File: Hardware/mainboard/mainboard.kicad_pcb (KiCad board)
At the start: 2 copper layers, 45 parts, among them J1 559592430, J2 B4B-EH-A, J3 B4B-EH-A, J4 B05B-XASK-1LFSN, J5 RST, J6 Conn_01x06_Socket, J7 SBH11-PBPC-D05-ST-BK, J9 USB_C_Receptacle_PowerOnly_24P, SW2 BOT, SW3 BOOT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

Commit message: pushing for the evening
didnt add much, just moved things around and fixed footprints
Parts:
- removed J5: RST, 1x02_jst_conn:CONN_B02B-XASK-1LFSN_JST
- added SW1: ON-BOARD, Button_Switch_SMD:SW_Tactile_SPST_NO_Straight_CK_PTS636Sx25SMTRLFS, F.Cu at (172.7, 86.4)
- SW3: footprint Connector_PinHeader_1.00mm:PinHeader_1x03_P1.00mm_Vertical -> Connector_PinHeader_2.54mm:PinHeader_1x03_P2.54mm_Vertical
- moved J2 148.0 mm to (229.9, 53.3), turned to 0 degrees
- moved J6 146.6 mm to (265.4, 87.2)
- moved R12 113.6 mm to (102.9, 60.0), turned to 90 degrees
- moved R1 110.3 mm to (232.4, 121.9), turned to 180 degrees
- moved U1 108.2 mm to (73.4, 138.9), turned to -90 degrees
- moved R11 107.5 mm to (102.9, 65.0), turned to 90 degrees
- moved R10 101.6 mm to (102.9, 70.1), turned to 90 degrees
- moved C8 98.6 mm to (152.7, 30.5), turned to 0 degrees
- moved R9 95.9 mm to (102.8, 75.2), turned to 90 degrees
- moved C7 95.0 mm to (147.6, 30.5), turned to 0 degrees
- moved C6 91.5 mm to (142.6, 30.5), turned to 0 degrees
- moved C5 87.9 mm to (137.5, 30.5), turned to 0 degrees
- moved C14 71.6 mm to (118.4, 150.6)
- moved J9 63.3 mm to (221.7, 149.9)
- moved D3 59.0 mm to (223.5, 139.7)
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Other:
- board text added: "3v3"
- board text added: "5v"
- board text added: "IR LEDs"
- board text added: "debouncing"
- board text added: "osc"
- board text added: "power in"
- board text added: "programming"
- board text added: "reset"
- board text added: "status led smd"

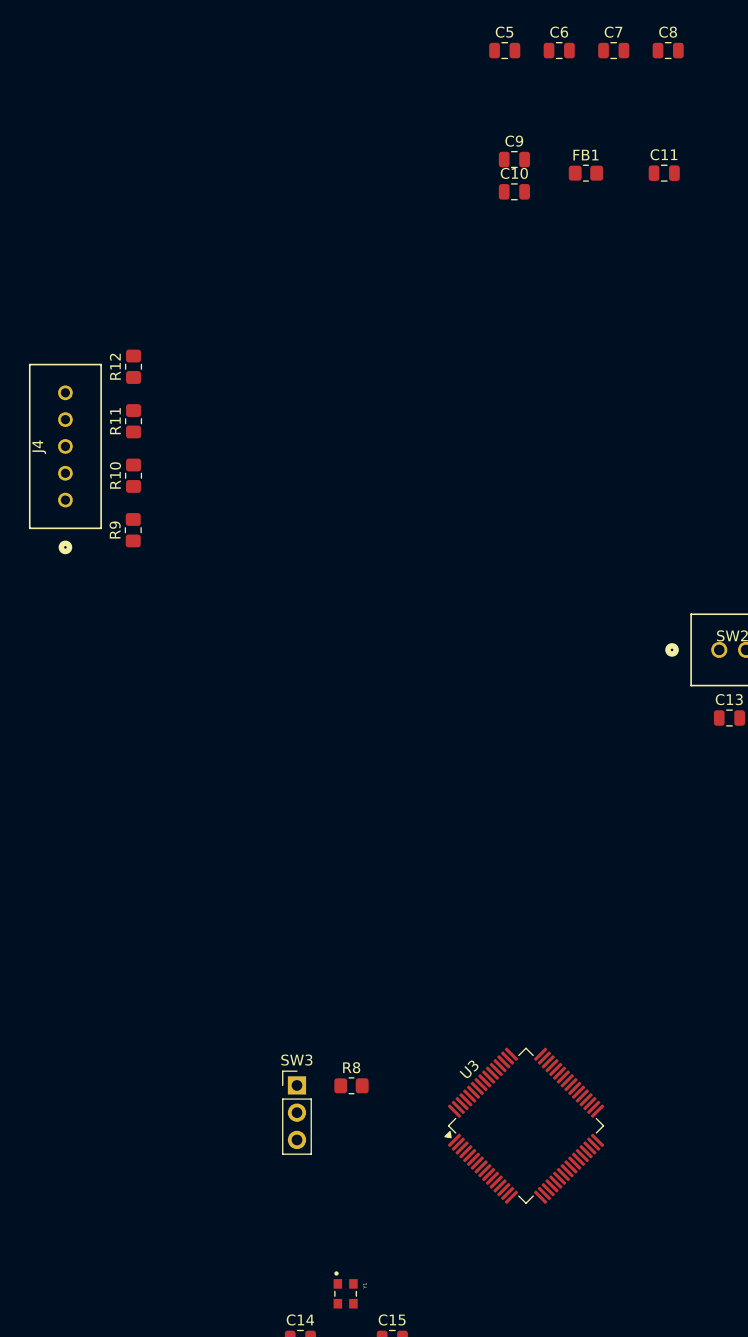
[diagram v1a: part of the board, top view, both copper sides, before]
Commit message: Lowkey forgot the start switch so i added that
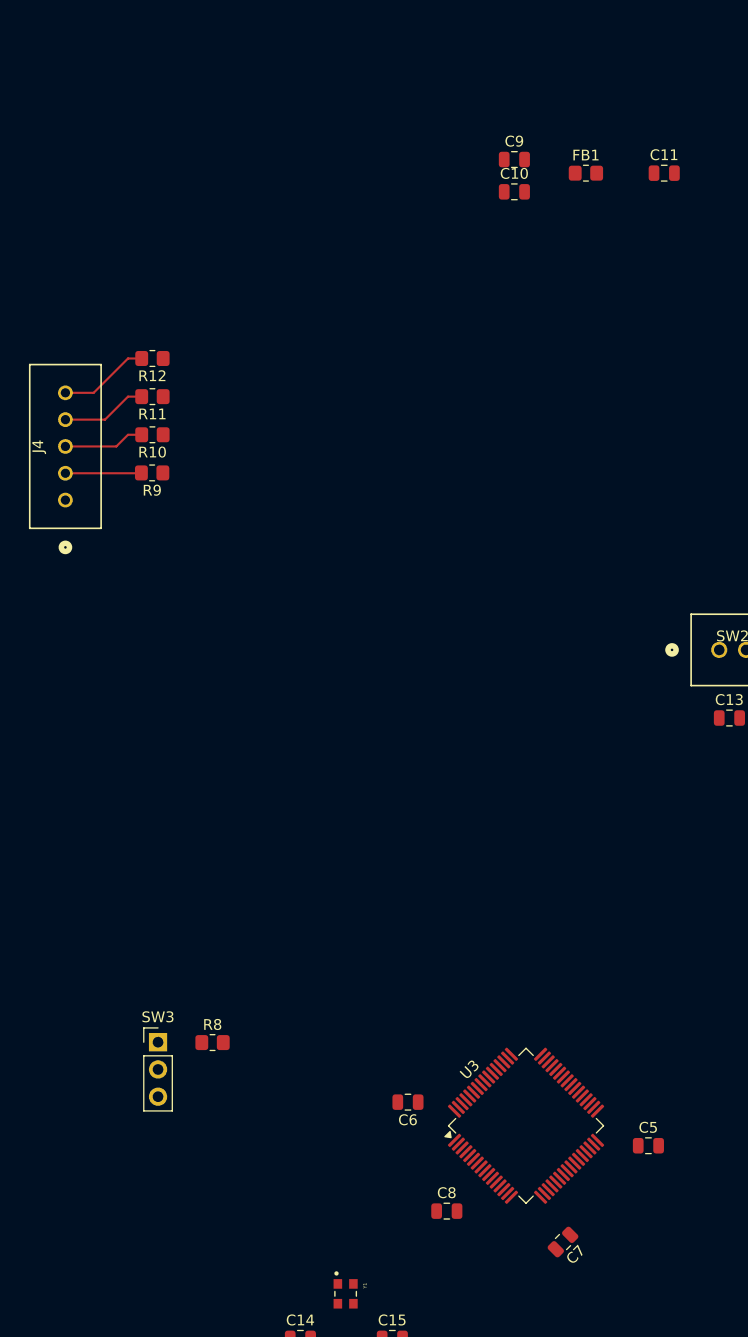
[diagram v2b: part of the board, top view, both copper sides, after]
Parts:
- moved C7 111.2 mm to (142.9, 141.6), turned to -135 degrees
- moved C8 110.2 mm to (132.1, 138.7)
- moved C5 103.0 mm to (150.9, 132.6)
- moved C6 99.1 mm to (128.5, 128.5), turned to 180 degrees
- moved R8 13.6 mm to (110.2, 123.0)
- moved SW3 13.6 mm to (105.2, 122.9)
- moved R9 5.63 mm to (104.6, 69.9), turned to 180 degrees
- moved R10 4.21 mm to (104.6, 66.3), turned to 180 degrees
- moved R11 2.89 mm to (104.6, 62.7), turned to 180 degrees
- moved R12 1.92 mm to (104.6, 59.2), turned to 180 degrees
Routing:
- net IR_4: track 0.00 -> 8.59 mm
- net IR_3: track 0.00 -> 8.15 mm
- net IR_2: track 0.00 -> 7.71 mm
- net IR_1: track 0.00 -> 7.25 mm

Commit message: layout
worked on the layput but im actively falling asleep while working on it so im going to call it a day
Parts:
- C1, C12, C13, C6, C7, C8: value C -> 100nF
- C10, C11: value C -> 1uF
- C14, C15: value C -> 10pF
- C2, C5: value C -> 10uF
- C3, C4: value C -> 22uF
- C9: value C -> 10nF
- D1, D3: value SMAZ5V1-13-F -> zener
- J6: footprint Connector_PinHeader_1.00mm:PinHeader_1x06_P1.00mm_Vertical -> Connector_PinHeader_2.54mm:PinHeader_1x06_P2.54mm_Vertical
- R1: value R_US -> 1k5
- R10, R11, R12, R9: value R_US -> 220
- R2, R3, R4, R5, R6, R7: value R_US -> 50
- R8: value R_US -> 10k
- moved J7 141.7 mm to (134.6, 174.0)
- moved D2 129.7 mm to (110.5, 160.1), turned to -90 degrees
- moved R1 126.3 mm to (110.5, 154.7), turned to -90 degrees
- moved J1 110.6 mm to (170.2, 138.3), turned to -90 degrees
- moved J6 110.1 mm to (156.0, 98.6)
- moved U2 99.1 mm to (119.4, 157.5), turned to 180 degrees
- moved U1 94.7 mm to (167.6, 129.9), turned to 90 degrees
- moved D1 94.4 mm to (143.5, 162.6), turned to -90 degrees
- moved C3 88.1 mm to (128.3, 153.7), turned to 90 degrees
- moved C4 85.4 mm to (128.3, 159.1), turned to -90 degrees
- moved C2 83.8 mm to (142.2, 154.9)
- moved C1 82.6 mm to (148.6, 154.9)
- moved D3 74.7 mm to (152.4, 162.6), turned to -90 degrees
- moved J4 73.8 mm to (100.3, 146.1)
- moved R9 73.8 mm to (108.4, 143.6)
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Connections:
- U3 pad 52: unconnected-(U3-PC11-Pad52) -> PC11
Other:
- board text removed: "osc"

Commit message: add layer
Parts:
- removed J9: USB_C_Receptacle_PowerOnly_24P, usbc_power_only:KUSBX-SMT-CS-6-BTR_KYC
- removed R10, R11, R12, R9: 220, Resistor_SMD:R_0805_2012Metric_Pad1.20x1.40mm_HandSolder
- removed R2, R3, R4, R5, R6, R7: 50, Resistor_SMD:R_0805_2012Metric_Pad1.20x1.40mm_HandSolder
- added J5: race start, BIG LIBRARY:1X03_JST, F.Cu at (156.0, 108.0)
- added J8: KUSBX-SMT-CS-6-BTR, usbc_power_only:KUSBX-SMT-CS-6-BTR_KYC, F.Cu at (100.5, 169.0)
- added R13: R_US, Resistor_SMD:R_0805_2012Metric_Pad1.20x1.40mm_HandSolder, F.Cu at (153.2, 113.5)
- added TP1: TestPoint, TestPoint:TestPoint_Keystone_5019_Minature, F.Cu at (65.0, 58.1)
- added TP2: TestPoint, TestPoint:TestPoint_Keystone_5019_Minature, F.Cu at (65.0, 62.0)
- added TP3: TestPoint, TestPoint:TestPoint_Keystone_5019_Minature, F.Cu at (65.0, 66.0)
- C6, C7, C8: moved to B.Cu
- J2: value B4B-EH-A -> status bot
- J3: value B4B-EH-A -> status eot
- J6: value Conn_01x06_Socket -> usb-ttl
- J7: value SBH11-PBPC-D05-ST-BK -> jtag
- U3: footprint Package_QFP:LQFP-64_10x10mm_P0.5mm -> STM32F091RCT-6:STM32F091RCT6-M
- moved J3 137.6 mm to (99.0, 111.0), turned to 90 degrees
- moved J2 136.7 mm to (106.0, 111.0), turned to 90 degrees
- moved C11 107.9 mm to (128.0, 147.0), turned to 90 degrees
- moved FB1 107.0 mm to (132.8, 148.2), turned to 180 degrees
- moved C9 102.9 mm to (130.2, 143.2), turned to 90 degrees
- moved C10 99.7 mm to (134.8, 143.2), turned to 90 degrees
- moved J6 75.8 mm to (91.0, 137.5), turned to 180 degrees
- moved SW2 63.4 mm to (159.6, 149.3), turned to -90 degrees
- moved J1 60.0 mm to (119.5, 106.2), turned to 0 degrees
- moved J7 54.6 mm to (100.5, 131.3), turned to -90 degrees
- moved D3 52.7 mm to (99.9, 158.4), turned to 180 degrees
- moved C13 49.1 mm to (152.0, 150.1), turned to 90 degrees
- moved SW1 48.5 mm to (158.9, 160.0), turned to 0 degrees
- moved D1 45.1 mm to (99.9, 151.0), turned to 180 degrees
- moved C1 41.2 mm to (107.5, 153.0), turned to -90 degrees
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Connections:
- C10 pad 2: GND -> Net-(U3-VDDA)
- C9 pad 2: GND -> Net-(U3-VDDA)
- U3 pad 13: GND -> Net-(U3-VDDA)
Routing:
- net PB10: track 0.00 -> 52.4 mm, vias 0 -> 2
- net SWDIO: track 0.00 -> 48.0 mm
- net SWCLK: track 0.00 -> 47.9 mm
- net PC11: track 0.00 -> 31.1 mm, vias 0 -> 2
- net PA0: track 0.00 -> 27.2 mm
- net PA2: track 0.00 -> 26.0 mm
- net PA1: track 0.00 -> 26.0 mm
- net PA7: track 0.00 -> 22.9 mm
- net PA6: track 0.00 -> 22.5 mm
- net PA5: track 0.00 -> 22.1 mm
- net PA3: track 0.00 -> 21.8 mm
- net PA4: track 0.00 -> 21.6 mm
- net PC10: track 0.00 -> 17.8 mm, vias 0 -> 1
- net Net-(U3-VDDA): track 0.00 -> 11.4 mm
- net +3.3V: track 0.00 -> 10.3 mm, vias 0 -> 3
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- added copper zone on In2.Cu, net +3.3V
- added copper zone on B.Cu, net GND
- added copper zone on F.Cu, net GND
- added copper zone on In1.Cu, net GND
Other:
- copper layers 2 -> 4

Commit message: routed traces
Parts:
- added REF**: MountingHole_4.3mm_M4, MountingHole:MountingHole_4.3mm_M4, F.Cu at (135.6, 85.9)
- added REF**: MountingHole_4.3mm_M4, MountingHole:MountingHole_4.3mm_M4, F.Cu at (66.3, 25.4)
- added REF**: MountingHole_4.3mm_M4, MountingHole:MountingHole_4.3mm_M4, F.Cu at (66.4, 85.9)
- added REF**: MountingHole_4.3mm_M4, MountingHole:MountingHole_4.3mm_M4, F.Cu at (135.6, 25.5)
- moved J6 93.5 mm to (65.3, 47.6), turned to 0 degrees
- moved C12 89.1 mm to (119.4, 75.9), turned to 180 degrees
- moved D2 88.1 mm to (92.8, 86.0)
- moved R1 88.1 mm to (87.4, 86.0)
- moved U2 88.1 mm to (90.2, 77.1)
- moved J4 87.7 mm to (103.1, 85.7)
- moved C3 86.9 mm to (86.7, 69.3)
- moved C4 86.9 mm to (92.1, 69.3)
- moved C5 86.9 mm to (92.1, 64.2)
- moved SW1 85.7 mm to (125.0, 81.3), turned to -90 degrees
- moved C1 85.0 mm to (80.8, 72.3)
- moved C2 85.0 mm to (80.8, 77.3)
- moved D1 85.0 mm to (73.2, 70.3)
- moved D3 85.0 mm to (73.2, 77.7)
- moved J8 84.3 mm to (76.7, 88.1)
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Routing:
- net RST: track 0.00 -> 86.9 mm, vias 0 -> 4
- net PB2: track 8.83 -> 66.8 mm, vias 2 -> 1
- net PC13: track 0.00 -> 51.7 mm, vias 0 -> 2
- net PC14: track 0.00 -> 51.3 mm, vias 0 -> 2
- net PC15: track 0.00 -> 51.0 mm, vias 0 -> 2
- net PB0: track 5.92 -> 55.1 mm, vias 2 -> 1
- net PC12: track 0.00 -> 48.4 mm, vias 0 -> 2
- net PB1: track 7.00 -> 54.0 mm
- net PD2: track 0.00 -> 46.5 mm, vias 0 -> 2
- net PA8: track 0.00 -> 41.2 mm, vias 0 -> 2
- net PA9: track 0.00 -> 37.0 mm, vias 0 -> 2
- net PC9: track 1.45 -> 37.9 mm, vias 1 -> 2
- net PA10: track 0.00 -> 33.1 mm
- net PC1: track 5.20 -> 38.3 mm, vias 1 -> 2
- net PC3: track 4.20 -> 35.9 mm, vias 1 -> 2
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- added copper zone on F.Cu, net +3.3V
- added copper zone on F.Cu, net /programming/5v5_in_jtag
- added copper zone on F.Cu, net /programming/5v5_usb
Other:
- board outline added: 78.3 x 69.6 mm
- board text added: "gnd"
- board text removed: "5v"
- board text removed: "debouncing"
- board text removed: "power in"
- board text removed: "programming"
- board text removed: "reset"
- board text removed: "status led smd"

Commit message: lowkey accidentally deleted everything but i brought a previous commit back since i am a true girlboss
like i deleted inner layers since i thought iw as looking at a diff board
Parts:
- moved J3 11.7 mm to (80.1, 24.4), turned to 0 degrees
- moved J2 6.78 mm to (65.5, 37.7)
- moved REF** 0.37 mm to (66.5, 25.7)
- moved REF** 0.36 mm to (135.4, 85.6)
- moved REF** 0.36 mm to (66.5, 85.6)
- moved REF** 0.24 mm to (135.4, 25.7)
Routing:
- net PC15: track 51.0 -> 72.1 mm, vias 2 -> 3
- net PC14: track 51.3 -> 69.8 mm, vias 2 -> 3
- net PC13: track 51.7 -> 68.4 mm
- net GND: track 25.1 -> 26.0 mm
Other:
- board size 78.3 x 69.6 mm -> 78 x 69.1 mm

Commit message: final push for the night
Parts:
- added G***: LOGO, LOGO, F.Cu at (89.2, 54.6)
- J2: value status bot -> status LEDs 1
- J3: value status eot -> status LEDs 2
- J8: footprint usbc_power_only:KUSBX-SMT-CS-6-BTR_KYC -> BIG LIBRARY:usb-c2
- SW2: value BOT -> BOT Switch
- moved J8 2.16 mm to (76.7, 86.0)
- moved J6 1.14 mm to (64.1, 47.6)
- moved J7 0.72 mm to (74.0, 56.2)
- moved C4 0.18 mm to (91.9, 69.3), turned to 180 degrees
- moved C9 0.16 mm to (102.9, 68.1)
- turned TP1 to -90 degrees
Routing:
- net PD2: track 46.5 -> 47.6 mm
- net PC12: track 48.4 -> 49.5 mm
- net SWDIO: track 46.5 -> 45.8 mm
- net SWCLK: track 46.2 -> 45.5 mm
- net RST: track 86.9 -> 86.2 mm
- net GND: track 26.0 -> 26.6 mm
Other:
- board text added: "GND"
- board text added: "PC12"
- board text added: "PD2"
- board text added: "REV 1"
- board text added: "RST"
- board text added: "Timer Mainboard"
- board text added: "pin 1"
- board text added: "↓"
